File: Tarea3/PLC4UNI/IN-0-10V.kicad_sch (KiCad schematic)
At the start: 0 parts

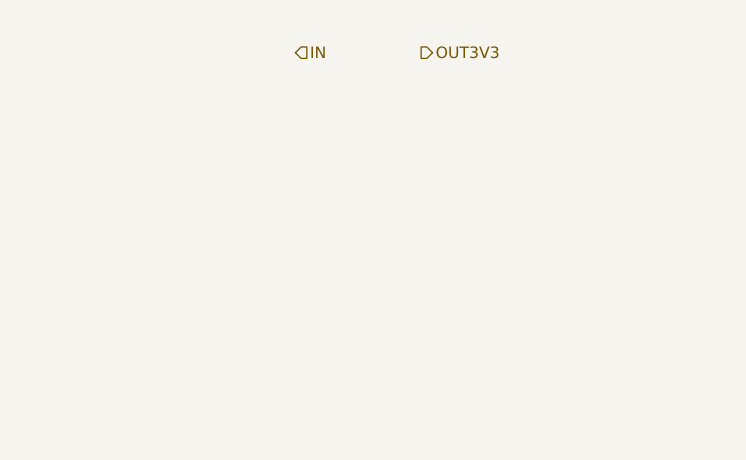
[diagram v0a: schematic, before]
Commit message: Cambio de directorio [Tarea2->CAD]
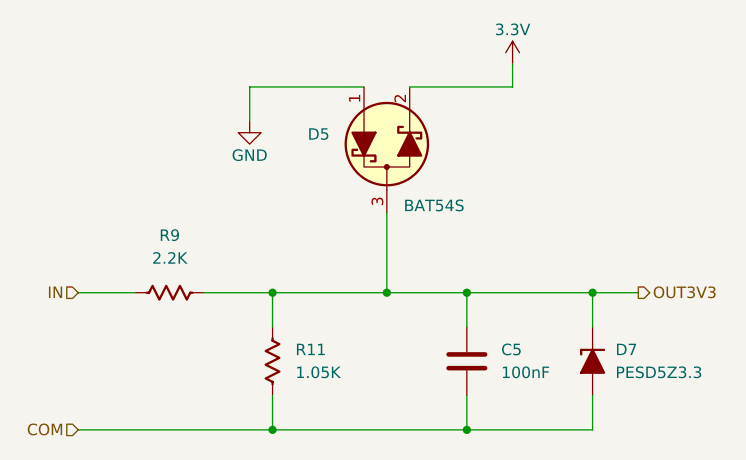
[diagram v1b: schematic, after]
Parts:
- added C5: 100nF, PCM_Capacitor_SMD_AKL:C_0603_1608Metric, symbol PCM_Capacitor_US_AKL:C_0603
- added D5: BAT54S, PCM_Package_TO_SOT_SMD_AKL:SOT-23, symbol PCM_Diode_Schottky_AKL:BAT54S
- added D7: PESD5Z3.3, PCM_Diode_SMD_AKL:D_SOD-523, symbol PCM_Diode_TVS_AKL:PESD5Z3.3
- added R11: 1.05K, PCM_Resistor_SMD_AKL:R_0603_1608Metric, symbol PCM_Resistor_US_AKL:R_0603
- added R9: 2.2K, PCM_Resistor_SMD_AKL:R_0603_1608Metric, symbol PCM_Resistor_US_AKL:R_0603
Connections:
- net IN: now also R9.1
- net OUT3V3: now also C5.1, D5.3 (C), D7.1 (K), R11.2, R9.2
- new net 3.3V: D5.2 (K)
- new net COM: C5.2, D7.2 (A), R11.1
- new net GND: D5.1 (A)
